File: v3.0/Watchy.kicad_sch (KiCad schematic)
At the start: 84 parts, among them J1 FPC24(0.5MM), J2 Conn_01x06, J3 Battery, J5 Conn_01x06, M1 Vibration_Motor, Q1 AO3400A, Q4 CJ2301, Q5 S8050, SW1 BTN, SW2 BTN, SW3 BTN, SW4 BTN, U1 CH340X, U2 ME6211C33M5G-N, U3 USBLC6-2P6, U4 BMA423, U5 TP4054, U6 PCF8563BS, U7 ESP32-S3, U8 SR2HARU, Y1 32.768KHz, Y3 40MHZ

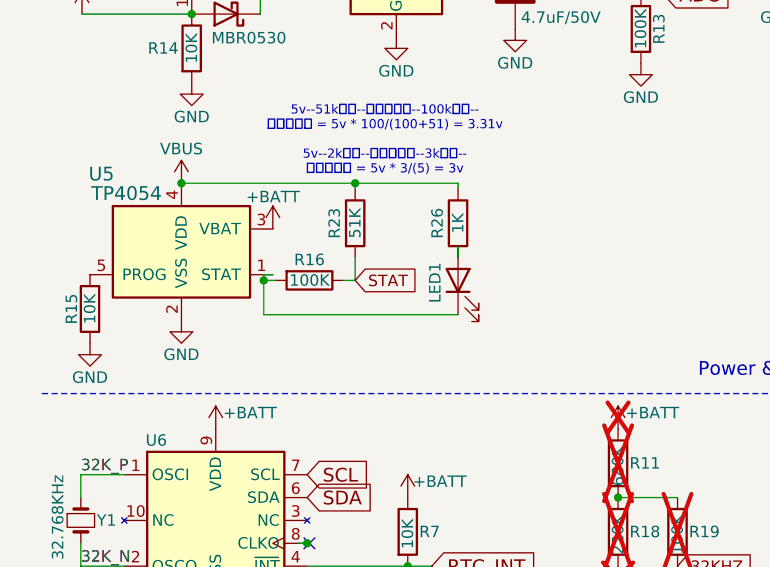
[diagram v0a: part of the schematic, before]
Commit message: delete R16,R23
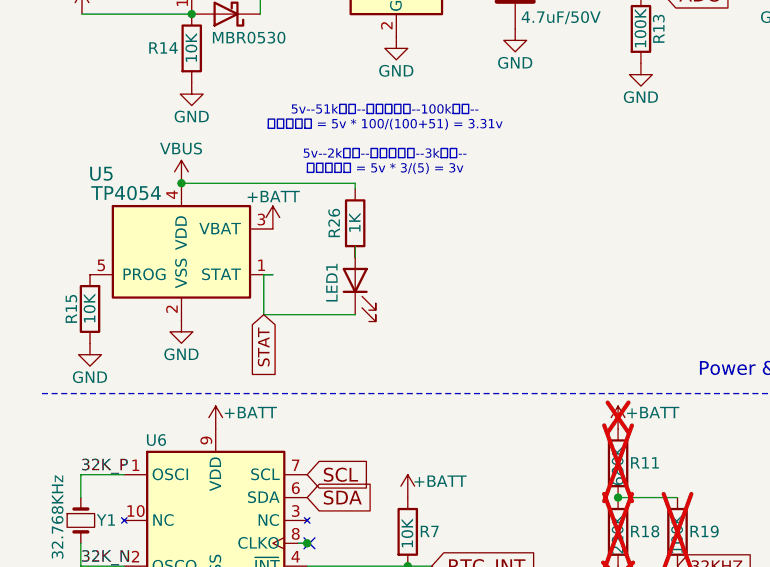
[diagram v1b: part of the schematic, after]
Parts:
- removed R16: 100K, Watchy:R0402-Frame, symbol Device:R
- removed R23: 51K, Watchy:R0402-Frame, symbol Device:R
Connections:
- net STAT: now also LED1.1 (K), U5.1 (STAT)
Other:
- moved on the sheet: LED1, R26
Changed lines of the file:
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@@
 	)
 	(junction
-		(at 46.99 145.415)
-		(diameter 0)
-		(color 0 0 0 0)
-	)
-	(junction
 		(at 143.51 182.88)
 		(diameter 0)
 		(color 0 0 0 0)
 	)
-	(junction
-		(at 36.83 156.21)
-		(diameter 0)
-		(color 0 0 0 0)
-	)
 	(no_connect
 		(at 41.91 185.42)
@@
 	(wire
 		(pts
-			(xy 58.42 153.67) (xy 58.42 152.4)
+			(xy 46.99 153.67) (xy 46.99 152.4)
 		)
 		(stroke
@@
 	(wire
 		(pts
-			(xy 38.1 156.21) (xy 36.83 156.21)
-		)
-		(stroke
-			(width 0)
-			(type default)
-		)
-	)
-	(wire
-		(pts
 			(xy 27.94 64.77) (xy 38.1 64.77)
 		)
@@
 	(wire
 		(pts
-			(xy 36.83 156.21) (xy 36.83 155.575)
-		)
-		(stroke
-			(width 0)
-			(type default)
-		)
-	)
-	(wire
-		(pts
 			(xy 59.182 118.999) (xy 65.024 118.999)
 		)
@@
 		)
 	)
-	(wire
-		(pts
-			(xy 46.99 153.67) (xy 46.99 156.21)
-		)
-		(stroke
-			(width 0)
-			(type default)
-		)
-	)
 	(polyline
 		(pts
@@
 		)
 	)
-	(wire
-		(pts
-			(xy 58.42 145.415) (xy 58.42 146.05)
-		)
-		(stroke
-			(width 0)
-			(type default)
-		)
-	)
 	(polyline
 		(pts
@@
 	(wire
 		(pts
-			(xy 58.42 145.415) (xy 46.99 145.415)
-		)
-		(stroke
-			(width 0)
-			(type default)
-		)
-	)
-	(wire
-		(pts
 			(xy 40.513 118.999) (xy 40.513 121.539)
 		)
@@
 	(wire
 		(pts
-			(xy 36.83 160.02) (xy 36.83 156.21)
+			(xy 36.83 155.575) (xy 36.83 160.02)
 		)
 		(stroke
@@
 		)
 	)
-	(wire
-		(pts
-			(xy 45.72 156.21) (xy 46.99 156.21)
-		)
-		(stroke
-			(width 0)
-			(type default)
-		)
-	)
 	(polyline
 		(pts
@@
 	(wire
 		(pts
-			(xy 58.42 160.02) (xy 36.83 160.02)
+			(xy 46.99 160.02) (xy 36.83 160.02)
 		)
 		(stroke
@@
 		)
 	)
-	(global_label "STAT"
-		(shape input)
-		(at 46.99 156.21 0)
-		(fields_autoplaced yes)
-		(effects
-			(font
-				(size 1.27 1.27)
-			)
-			(justify left)
-		)
-		(property "Intersheetrefs" "${INTERSHEET_REFS}"
-			(at 53.5543 156.21 0)
-			(effects
-				(font
-					(size 1.27 1.27)
-				)
-				(justify left)
-				(hide yes)
-			)
-		)
-	)
 	(global_label "BTN_4"
 		(shape input)
@@
 		)
 	)
+	(global_label "STAT"
+		(shape input)
+		(at 36.83 160.02 270)
+		(fields_autoplaced yes)
+		(effects
+			(font
+				(size 1.27 1.27)
+			)
+			(justify right)
+		)
+		(property "Intersheetrefs" "${INTERSHEET_REFS}"
+			(at 36.83 166.5843 90)
+			(effects
+				(font
+					(size 1.27 1.27)
+				)
+				(justify right)
+				(hide yes)
+			)
+		)
+	)
 	(global_label "RX"
 		(shape input)
@@
 	)
 	(symbol
-		(lib_id "Device:R")
-		(at 41.91 156.21 270)
-		(unit 1)
-		(exclude_from_sim no)
-		(in_bom yes)
-		(on_board yes)
-		(dnp no)
-		(property "Reference" "R16"
-			(at 41.91 153.924 90)
-			(effects
-				(font
-					(size 1.27 1.27)
-				)
-			)
-		)
-		(property "Value" "100K"
-			(at 41.91 156.21 90)
-			(effects
-				(font
-					(size 1.27 1.27)
-				)
-			)
-		)
-		(property "Footprint" "Watchy:R0402-Frame"
-			(at 41.91 154.432 90)
-			(effects
-				(font
-					(size 1.27 1.27)
-				)
-				(hide yes)
-			)
-		)
-		(property "Datasheet" ""
-			(at 41.91 156.21 0)
-			(effects
-				(font
-					(size 1.27 1.27)
-				)
-				(hide yes)
-			)
-		)
-		(property "Description" ""
-			(at 41.91 156.21 0)
-			(effects
-				(font
-					(size 1.27 1.27)
-				)
-				(hide yes)
-			)
-		)
-		(pin "1"
-		)
-		(pin "2"
-		)
-		(instances
-			(project ""
-				(path "/4d1a201a-55a3-4008-8b69-98c973b46b97"
-					(reference "R16")
-					(unit 1)
-				)
-			)
-		)
-	)
-	(symbol
 		(lib_id "Watchy-rescue:GND-power")
 		(at 27.686 160.655 0)
@@
 	(symbol
 		(lib_id "Device:LED")
-		(at 58.42 156.21 90)
+		(at 46.99 156.21 90)
 		(unit 1)
 		(exclude_from_sim no)
@@
 		(dnp no)
 		(property "Reference" "LED1"
-			(at 55.88 156.464 0)
+			(at 44.45 156.464 0)
 			(effects
 				(font
@@
 		)
 		(property "Value" "LED"
-			(at 55.88 160.274 0)
+			(at 44.45 160.274 0)
 			(effects
 				(font
@@
 		)
 		(property "Footprint" "Watchy:LED_0402_1005Metric"
-			(at 58.42 156.21 0)
+			(at 46.99 156.21 0)
 			(effects
 				(font
@@
 		)
 		(property "Datasheet" "~"
-			(at 58.42 156.21 0)
+			(at 46.99 156.21 0)
 			(effects
 				(font
@@
 		)
 		(property "Description" "Light emitting diode"
-			(at 58.42 156.21 0)
+			(at 46.99 156.21 0)
 			(effects
 				(font
@@
 	(symbol
 		(lib_id "Device:R")
-		(at 58.42 149.86 0)
+		(at 46.99 149.86 0)
 		(unit 1)
 		(exclude_from_sim no)
@@
 		(dnp no)
 		(property "Reference" "R26"
-			(at 56.134 149.86 90)
+			(at 44.704 149.86 90)
 			(effects
 				(font
@@
 		)
 		(property "Value" "1K"
-			(at 58.42 149.86 90)
+			(at 46.99 149.86 90)
 			(effects
 				(font
@@
 		)
 		(property "Footprint" "Watchy:R0402-Frame"
-			(at 56.642 149.86 90)
+			(at 45.212 149.86 90)
 			(effects
 				(font
@@
 		)
 		(property "Datasheet" ""
-			(at 58.42 149.86 0)
+			(at 46.99 149.86 0)
 			(effects
 				(font
@@
 		)
 		(property "Description" ""
-			(at 58.42 149.86 0)
+			(at 46.99 149.86 0)
 			(effects
 				(font
@@
 					(unit 1)
 				)
-			)
-		)
-	)
-	(symbol
-		(lib_id "Device:R")
-		(at 46.99 149.86 0)
-		(unit 1)
-		(exclude_from_sim no)
-		(in_bom yes)
-		(on_board yes)
-		(dnp no)
-		(property "Reference" "R23"
-			(at 44.704 149.86 90)
-			(effects
-				(font
-					(size 1.27 1.27)
-				)
-			)
-		)
-		(property "Value" "51K"
-			(at 46.99 149.86 90)
-			(effects
-				(font
-					(size 1.27 1.27)
-				)
-			)
-		)
-		(property "Footprint" "Watchy:R0402-Frame"
-			(at 45.212 149.86 90)
-			(effects
-				(font
-					(size 1.27 1.27)
-				)
-				(hide yes)
-			)
-		)
-		(property "Datasheet" ""
-			(at 46.99 149.86 0)
-			(effects
-				(font
-					(size 1.27 1.27)
-				)
-				(hide yes)
-			)
-		)
-		(property "Description" ""
-			(at 46.99 149.86 0)
-			(effects
-				(font
-					(size 1.27 1.27)
-				)
-				(hide yes)
-			)
-		)
-		(pin "1"
-		)
-		(pin "2"
-		)
-		(instances
-			(project "Watchy"
-				(path "/4d1a201a-55a3-4008-8b69-98c973b46b97"
-					(reference "R23")
-					(unit 1)
-				)
